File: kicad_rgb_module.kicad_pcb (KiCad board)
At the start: 2 copper layers, 25 x 25 mm, 29 parts, among them J1 Conn_HackConnect, SW1 TS-1088-AR02016, U1 STM32G030F6P6, U2 NCP114ASN330T1G

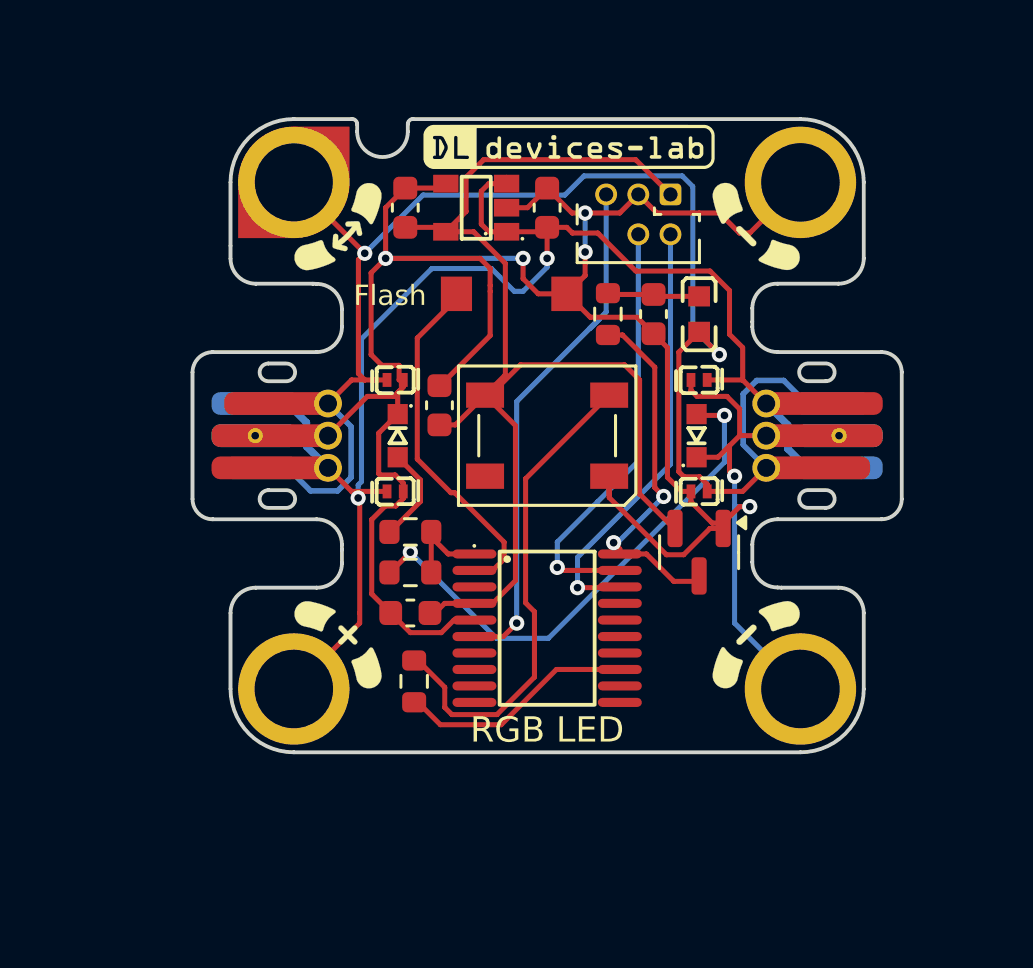
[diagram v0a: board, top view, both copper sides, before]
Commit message: meta/ dir required for template in Kicad
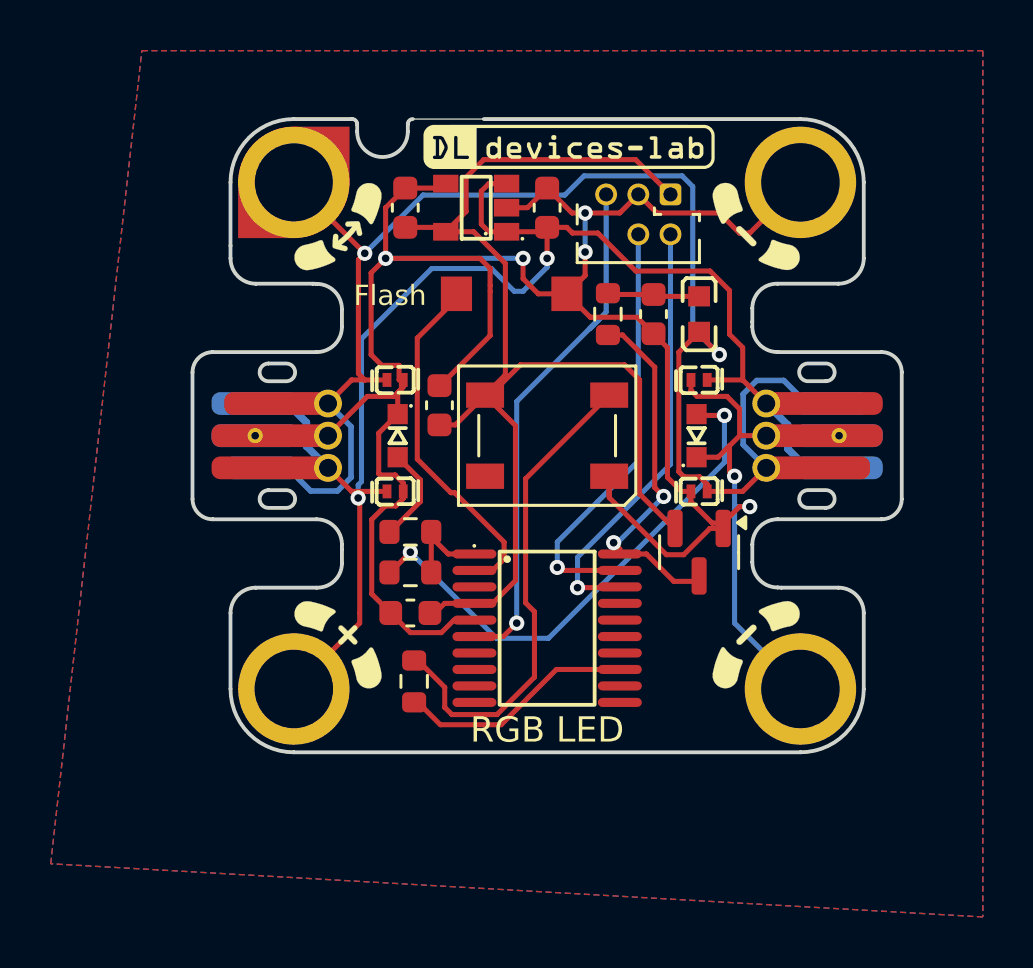
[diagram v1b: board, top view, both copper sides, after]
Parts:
- C5: value 1uF -> 2uF
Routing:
- added copper zone on B.Cu, net GND
- added copper zone on F.Cu, net GND
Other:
- outline, holes or cut-outs redrawn

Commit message: reverting unncessary change to .kicad_* files & sym-lib-table
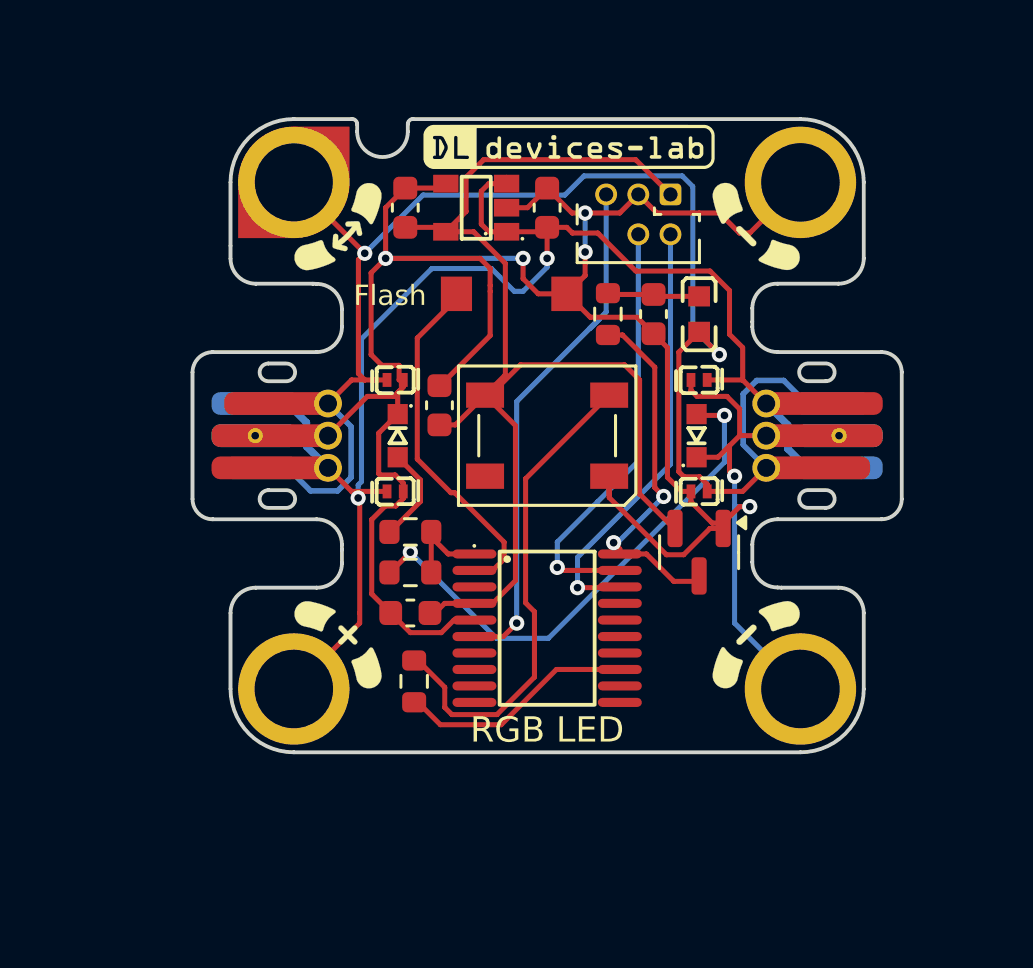
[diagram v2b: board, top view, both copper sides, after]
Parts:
- C5: value 2uF -> 1uF
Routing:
- removed copper zone on B.Cu, net GND
- removed copper zone on F.Cu, net GND
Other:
- outline, holes or cut-outs redrawn
